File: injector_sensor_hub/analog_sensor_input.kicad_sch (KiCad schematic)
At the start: 24 parts, among them J3 Conn_01x02_Female-Connector, J4 Conn_01x02_Female-Connector, J5 Conn_01x02_Female-Connector, J6 Conn_01x02_Female-Connector

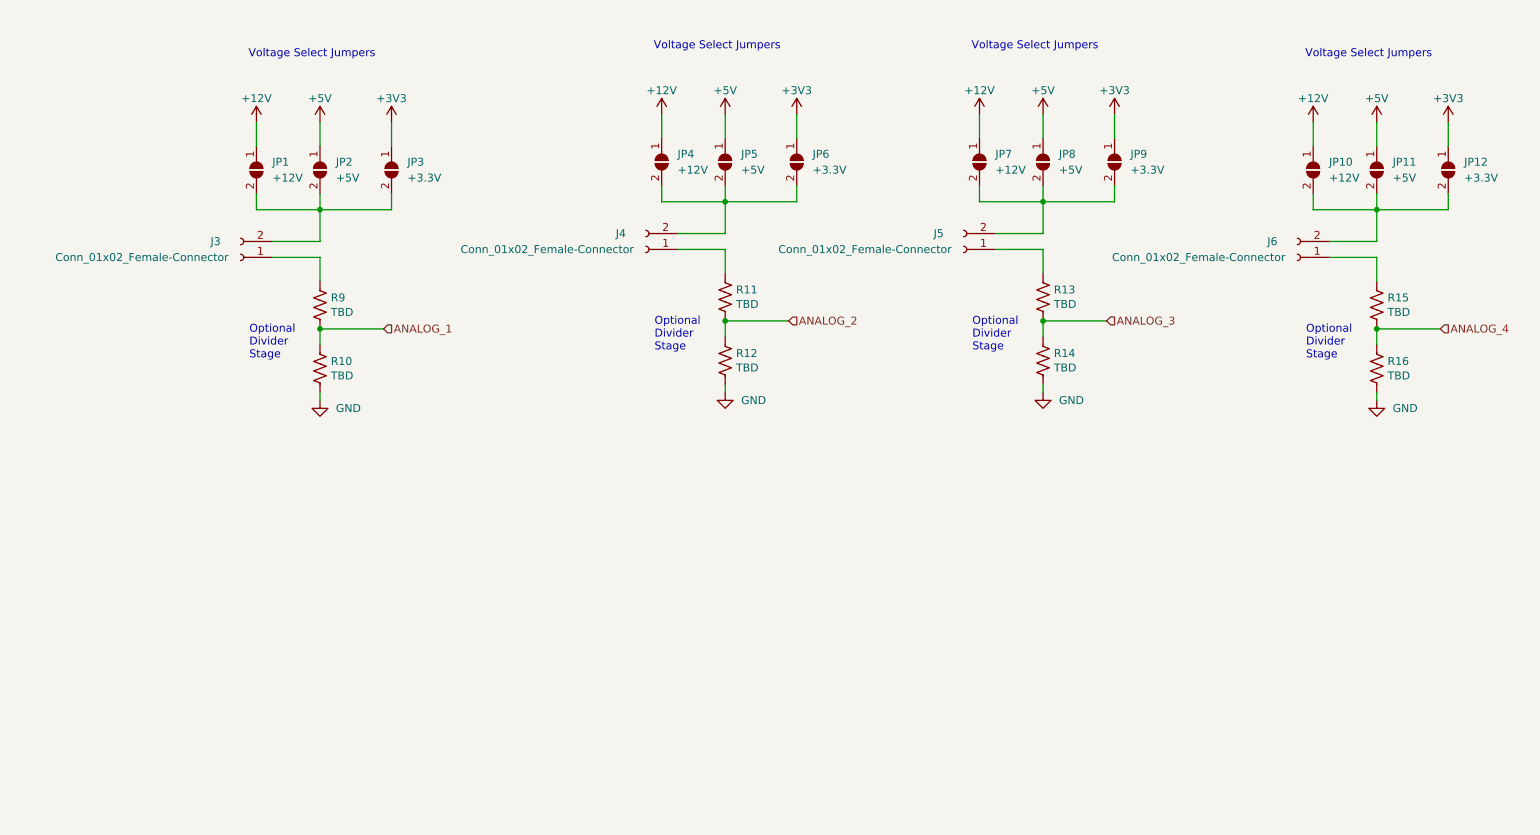
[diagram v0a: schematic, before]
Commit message: Add schematics
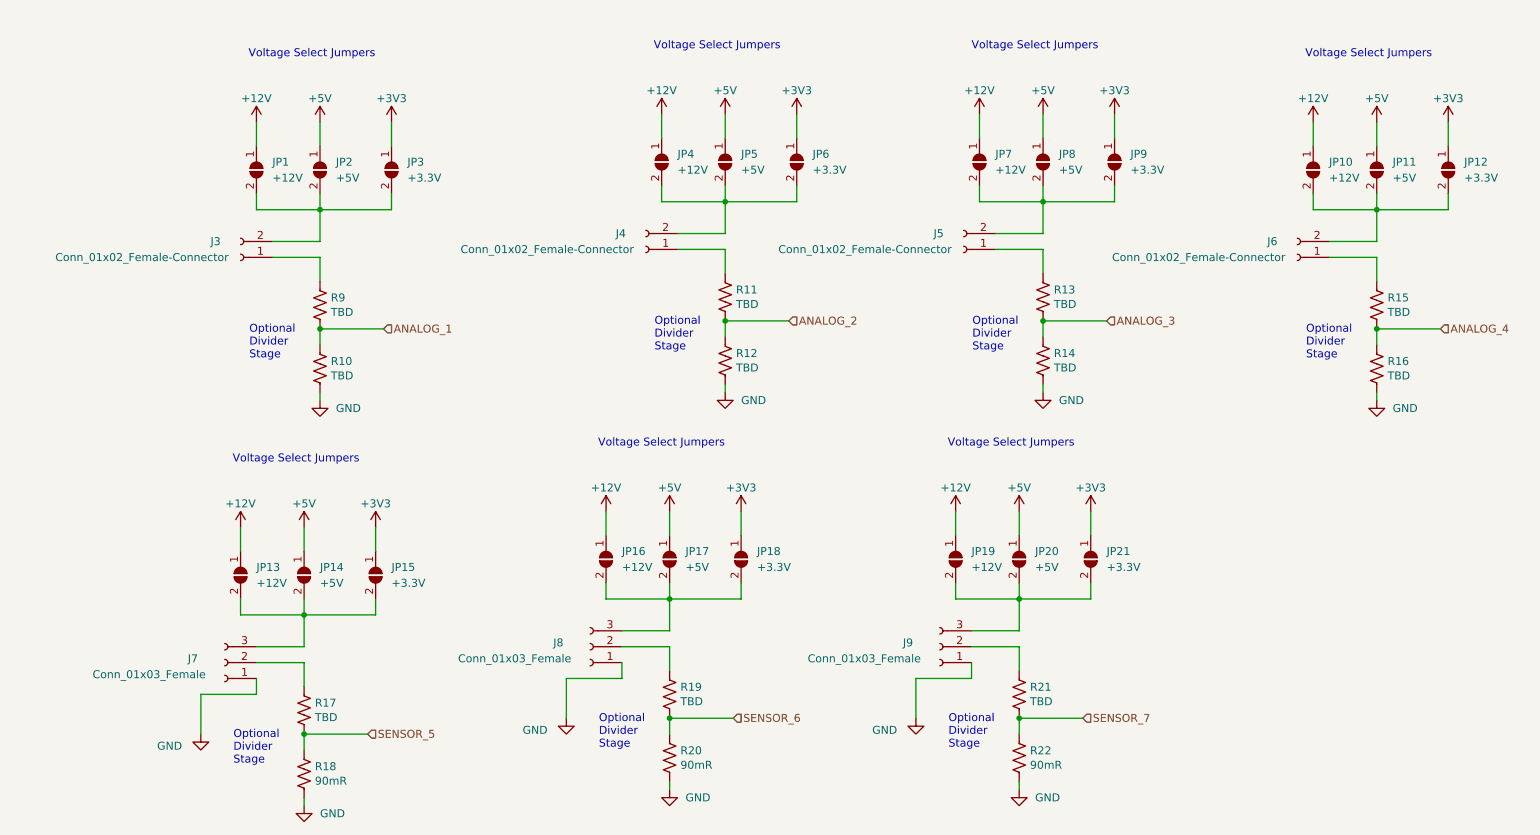
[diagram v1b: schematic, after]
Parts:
- added J7, J8, J9: Conn_01x03_Female, Connector_JST:JST_PH_S3B-PH-K_1x03_P2.00mm_Horizontal, symbol Connector:Conn_01x03_Female
- added JP13, JP16, JP19: +12V, Jumper:SolderJumper-2_P1.3mm_Open_Pad1.0x1.5mm, symbol Jumper:SolderJumper_2_Open
- added JP14, JP17, JP20: +5V, Jumper:SolderJumper-2_P1.3mm_Open_Pad1.0x1.5mm, symbol Jumper:SolderJumper_2_Open
- added JP15, JP18, JP21: +3.3V, Jumper:SolderJumper-2_P1.3mm_Open_Pad1.0x1.5mm, symbol Jumper:SolderJumper_2_Open
- added R17, R19, R21: TBD, Resistor_SMD:R_0805_2012Metric_Pad1.20x1.40mm_HandSolder, symbol Device:R_US
- added R18, R20, R22: 90mR, Resistor_SMD:R_0805_2012Metric_Pad1.20x1.40mm_HandSolder, symbol Device:R_US
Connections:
- net +12V: now also JP13.1 (A), JP16.1 (A), JP19.1 (A)
- net +3V3: now also JP15.1 (A), JP18.1 (A), JP21.1 (A)
- net +5V: now also JP14.1 (A), JP17.1 (A), JP20.1 (A)
- net GND: now also J7.1 (Pin_1), J8.1 (Pin_1), J9.1 (Pin_1), R18.2, R20.2, R22.2
- new net: J7.2 (Pin_2), R17.1
- new net: J8.2 (Pin_2), R19.1
- new net: J8.3 (Pin_3), JP16.2 (B), JP17.2 (B), JP18.2 (B)
- new net: J9.2 (Pin_2), R21.1
- new net: J9.3 (Pin_3), JP19.2 (B), JP20.2 (B), JP21.2 (B)
- new net: J7.3 (Pin_3), JP13.2 (B), JP14.2 (B), JP15.2 (B)
- new net SENSOR_5: R17.2, R18.1
- new net SENSOR_6: R19.2, R20.1
- new net SENSOR_7: R21.2, R22.1

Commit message: updates w ash
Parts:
- added J11: Conn_01x03_Female, Connector_JST:JST_PH_S3B-PH-K_1x03_P2.00mm_Horizontal, symbol Connector:Conn_01x03_Female
- added JP22: +12V, Jumper:SolderJumper-2_P1.3mm_Open_Pad1.0x1.5mm, symbol Jumper:SolderJumper_2_Open
- added JP23: +5V, Jumper:SolderJumper-2_P1.3mm_Open_Pad1.0x1.5mm, symbol Jumper:SolderJumper_2_Open
- added JP24: +3.3V, Jumper:SolderJumper-2_P1.3mm_Open_Pad1.0x1.5mm, symbol Jumper:SolderJumper_2_Open
- added R1: TBD, Resistor_SMD:R_0805_2012Metric_Pad1.20x1.40mm_HandSolder, symbol Device:R_US
- added R2: 90mR, Resistor_SMD:R_0805_2012Metric_Pad1.20x1.40mm_HandSolder, symbol Device:R_US
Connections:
- net +12V: now also JP22.1 (A)
- net +3V3: now also JP24.1 (A)
- net +5V: now also JP23.1 (A)
- net GND: now also J11.1 (Pin_1), R2.2
- new net: J11.2 (Pin_2), R1.1
- new net: J11.3 (Pin_3), JP22.2 (B), JP23.2 (B), JP24.2 (B)
- new net SENSOR_8: R1.2, R2.1

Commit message: final changes, tidy up schematic
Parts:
- R18, R2, R20, R22: value 90mR -> TBD
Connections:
- net ANALOG_1 renamed 2ANALOG_1
- net ANALOG_2 renamed 2ANALOG_2
- net ANALOG_3 renamed 2ANALOG_3
- net ANALOG_4 renamed 2ANALOG_4
- net SENSOR_5 renamed 3ANALOG_1
- net SENSOR_6 renamed 3ANALOG_2
- net SENSOR_7 renamed 3ANALOG_3
- net SENSOR_8 renamed 3ANALOG_4
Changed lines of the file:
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@@
 		)
 	)
-	(hierarchical_label "ANALOG_2"
-		(shape input)
+	(hierarchical_label "3ANALOG_3"
+		(shape output)
+		(at 199.39 134.62 0)
+		(fields_autoplaced yes)
+		(effects
+			(font
+				(size 1.27 1.27)
+			)
+			(justify left)
+		)
+	)
+	(hierarchical_label "3ANALOG_1"
+		(shape output)
+		(at 85.09 137.16 0)
+		(fields_autoplaced yes)
+		(effects
+			(font
+				(size 1.27 1.27)
+			)
+			(justify left)
+		)
+	)
+	(hierarchical_label "3ANALOG_4"
+		(shape output)
+		(at 256.54 135.89 0)
+		(fields_autoplaced yes)
+		(effects
+			(font
+				(size 1.27 1.27)
+			)
+			(justify left)
+		)
+	)
+	(hierarchical_label "2ANALOG_3"
+		(shape output)
+		(at 203.2 71.12 0)
+		(fields_autoplaced yes)
+		(effects
+			(font
+				(size 1.27 1.27)
+			)
+			(justify left)
+		)
+	)
+	(hierarchical_label "2ANALOG_2"
+		(shape output)
 		(at 152.4 71.12 0)
 		(fields_autoplaced yes)
@@
 		)
 	)
-	(hierarchical_label "SENSOR_8"
-		(shape input)
-		(at 256.54 135.89 0)
-		(fields_autoplaced yes)
-		(effects
-			(font
-				(size 1.27 1.27)
-			)
-			(justify left)
-		)
-	)
-	(hierarchical_label "ANALOG_3"
-		(shape input)
-		(at 203.2 71.12 0)
-		(fields_autoplaced yes)
-		(effects
-			(font
-				(size 1.27 1.27)
-			)
-			(justify left)
-		)
-	)
-	(hierarchical_label "SENSOR_5"
-		(shape input)
-		(at 85.09 137.16 0)
-		(fields_autoplaced yes)
-		(effects
-			(font
-				(size 1.27 1.27)
-			)
-			(justify left)
-		)
-	)
-	(hierarchical_label "ANALOG_1"
-		(shape input)
+	(hierarchical_label "2ANALOG_1"
+		(shape output)
 		(at 87.63 72.39 0)
 		(fields_autoplaced yes)
@@
 		)
 	)
-	(hierarchical_label "ANALOG_4"
-		(shape input)
+	(hierarchical_label "3ANALOG_2"
+		(shape output)
+		(at 143.51 134.62 0)
+		(fields_autoplaced yes)
+		(effects
+			(font
+				(size 1.27 1.27)
+			)
+			(justify left)
+		)
+	)
+	(hierarchical_label "2ANALOG_4"
+		(shape output)
 		(at 256.54 72.39 0)
 		(fields_autoplaced yes)
@@
 		)
 	)
-	(hierarchical_label "SENSOR_7"
-		(shape input)
-		(at 199.39 134.62 0)
-		(fields_autoplaced yes)
-		(effects
-			(font
-				(size 1.27 1.27)
-			)
-			(justify left)
-		)
-	)
-	(hierarchical_label "SENSOR_6"
-		(shape input)
-		(at 143.51 134.62 0)
-		(fields_autoplaced yes)
-		(effects
-			(font
-				(size 1.27 1.27)
-			)
-			(justify left)
-		)
-	)
 	(symbol
 		(lib_id "power:GND")
@@
 			)
 		)
-		(property "Value" "90mR"
+		(property "Value" "TBD"
 			(at 135.0772 142.113 0)
 			(effects
@@
 			)
 		)
-		(property "Value" "90mR"
+		(property "Value" "TBD"
 			(at 190.9572 142.113 0)
 			(effects
@@
 			)
 		)
-		(property "Value" "90mR"
+		(property "Value" "TBD"
 			(at 76.6572 144.653 0)
 			(effects
@@
 			)
 		)
-		(property "Value" "90mR"
+		(property "Value" "TBD"
 			(at 248.1072 143.383 0)
 			(effects

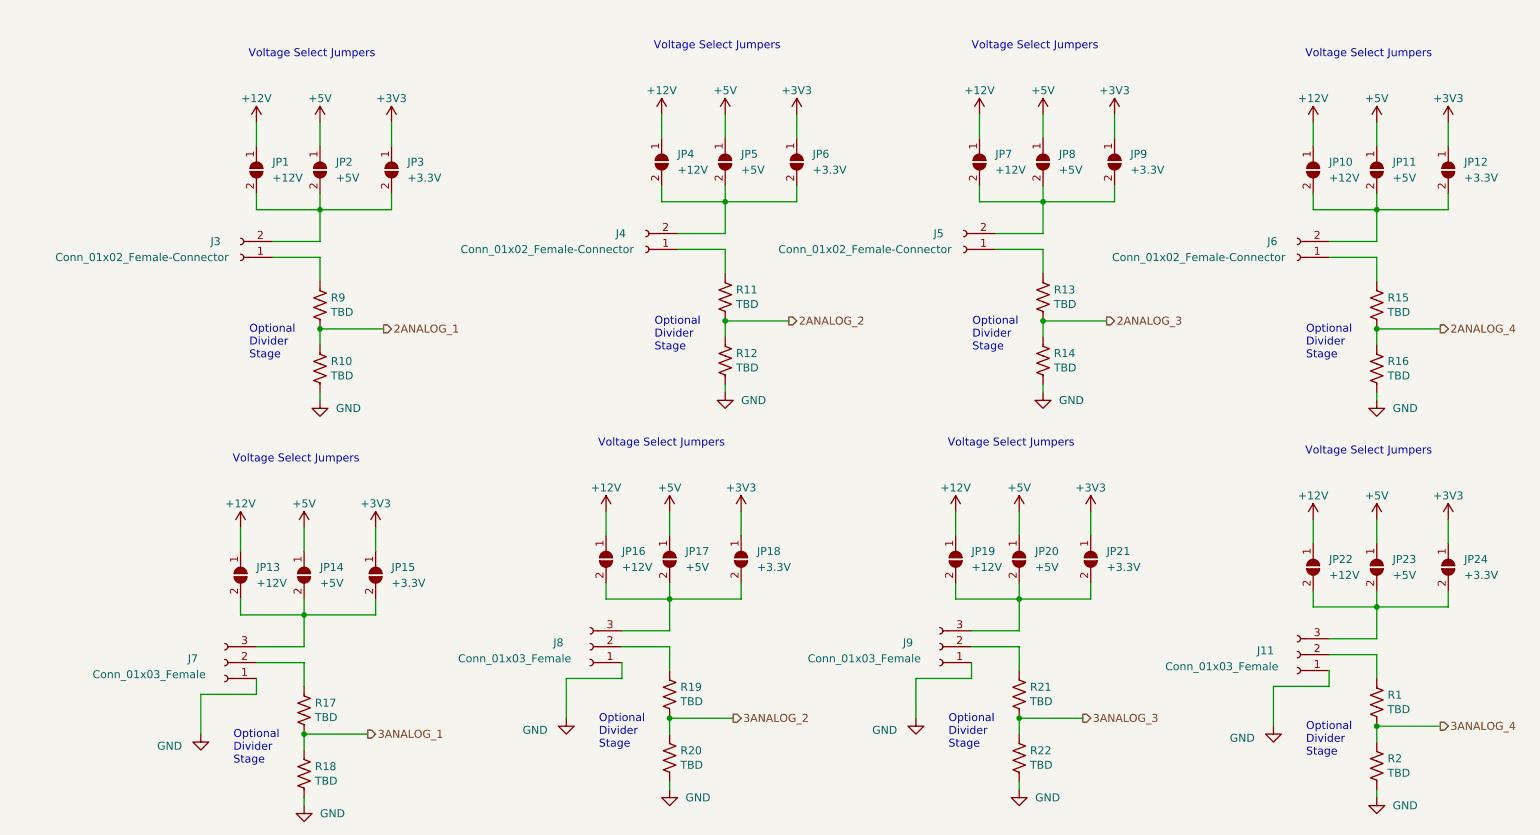
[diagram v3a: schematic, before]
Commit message: changed from 3v3 to 5v
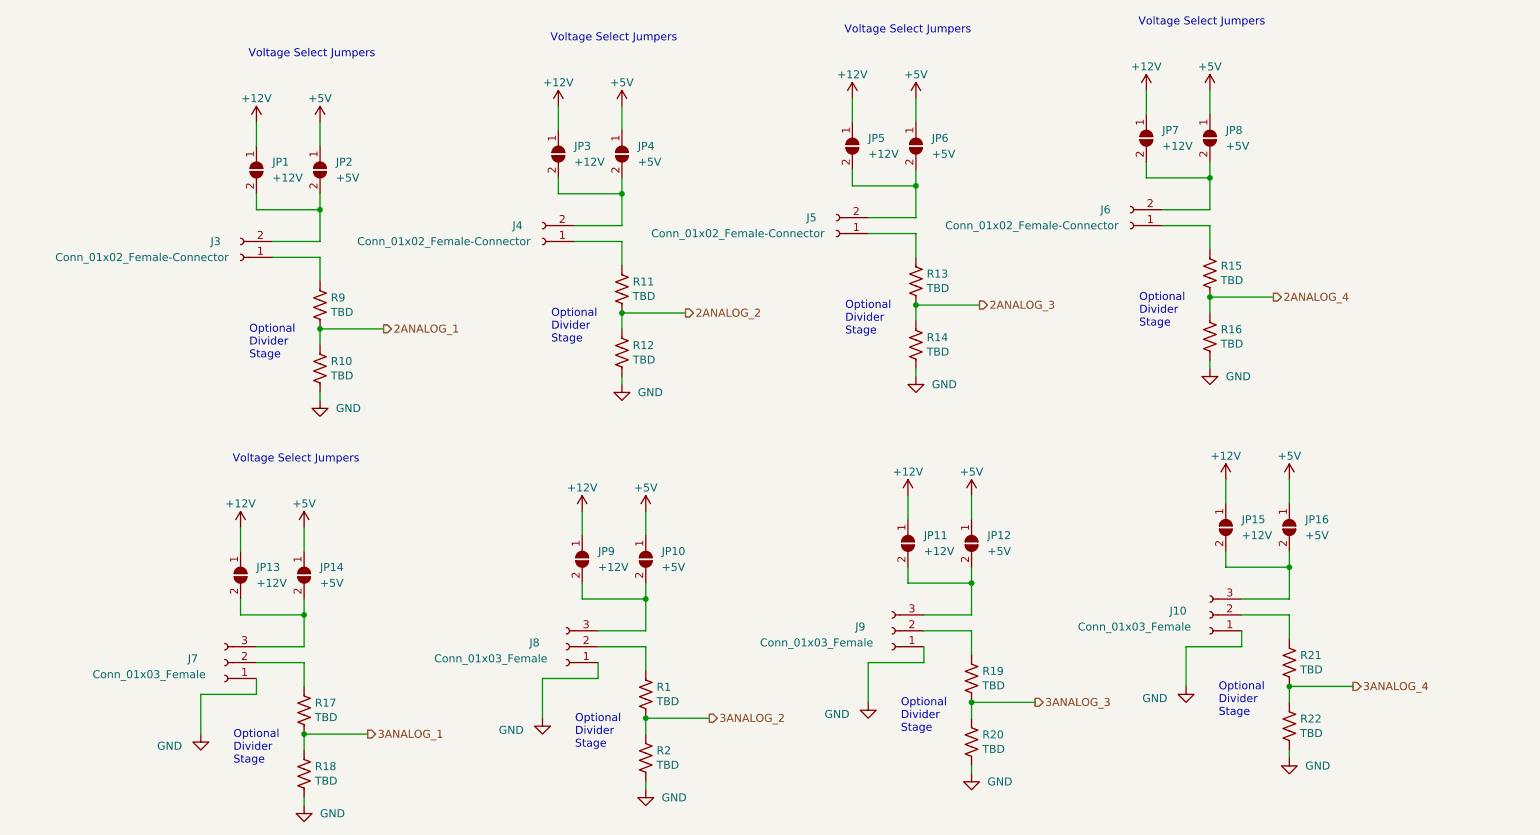
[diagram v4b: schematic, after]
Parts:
- removed J11: Conn_01x03_Female, Connector_JST:JST_PH_S3B-PH-K_1x03_P2.00mm_Horizontal, symbol Connector:Conn_01x03_Female
- removed JP17, JP20, JP23: +5V, Jumper:SolderJumper-2_P1.3mm_Open_Pad1.0x1.5mm, symbol Jumper:SolderJumper_2_Open
- removed JP18, JP21, JP24: +3.3V, Jumper:SolderJumper-2_P1.3mm_Open_Pad1.0x1.5mm, symbol Jumper:SolderJumper_2_Open
- removed JP19, JP22: +12V, Jumper:SolderJumper-2_P1.3mm_Open_Pad1.0x1.5mm, symbol Jumper:SolderJumper_2_Open
- added J10: Conn_01x03_Female, Connector_JST:JST_PH_S3B-PH-K_1x03_P2.00mm_Horizontal, symbol Connector:Conn_01x03_Female
- JP10, JP16, JP4: value +12V -> +5V
- JP11, JP5: value +5V -> +12V
- JP12, JP6: value +3.3V -> +5V
- JP15, JP3, JP9: value +3.3V -> +12V
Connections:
- net +12V: now also JP11.1 (A), JP15.1 (A), JP3.1 (A), JP5.1 (A), JP9.1 (A); no longer JP10.1 (A), JP16.1 (A), JP4.1 (A)
- net +5V: now also JP10.1 (A), JP12.1 (A), JP16.1 (A), JP4.1 (A), JP6.1 (A); no longer JP11.1 (A), JP5.1 (A)
- net 3ANALOG_2: now also R1.2, R2.1; no longer R19.2, R20.1
- net 3ANALOG_3: now also R19.2, R20.1; no longer R21.2, R22.1
- net 3ANALOG_4: now also R21.2, R22.1; no longer R1.2, R2.1
- net GND: now also J10.1 (Pin_1)
- net at J3.2 (Pin_2), JP1.2 (B), JP2.2 (B): no longer JP3.2 (B)
- net at R1.1: now also J8.2 (Pin_2)
- net at R19.1: now also J9.2 (Pin_2); no longer J8.2 (Pin_2)
- net at J8.3 (Pin_3): now also JP10.2 (B), JP9.2 (B); no longer JP16.2 (B)
- net at R21.1: now also J10.2 (Pin_2); no longer J9.2 (Pin_2)
- net at J9.3 (Pin_3): now also JP11.2 (B), JP12.2 (B)
- net at J4.2 (Pin_2), JP4.2 (B): now also JP3.2 (B); no longer JP5.2 (B), JP6.2 (B)
- net at JP7.2 (B), JP8.2 (B): now also J6.2 (Pin_2); no longer J5.2 (Pin_2), JP9.2 (B)
- net at J7.3 (Pin_3), JP13.2 (B), JP14.2 (B): no longer JP15.2 (B)
- removed net +3V3: JP12.1 (A), JP15.1 (A), JP3.1 (A), JP6.1 (A), JP9.1 (A)
- new net: J5.2 (Pin_2), JP5.2 (B), JP6.2 (B)
- new net: J10.3 (Pin_3), JP15.2 (B), JP16.2 (B)

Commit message: revert changes to daq and propulsion board
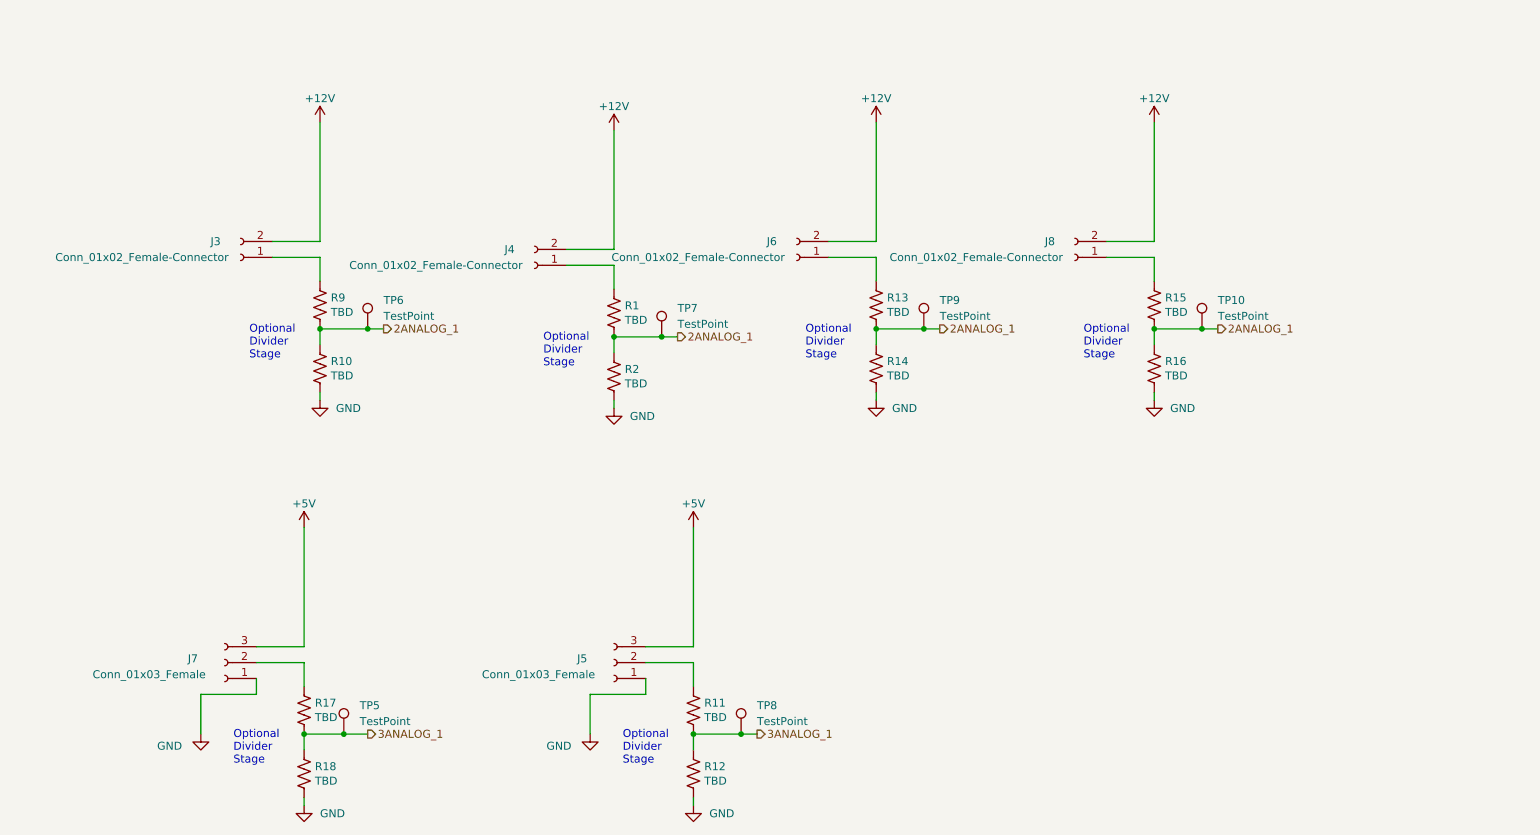
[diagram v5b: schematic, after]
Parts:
- removed J10, J8, J9: Conn_01x03_Female, Connector_JST:JST_PH_S3B-PH-K_1x03_P2.00mm_Horizontal, symbol Connector:Conn_01x03_Female
- removed J5: Conn_01x02_Female-Connector, Connector_JST:JST_PH_S2B-PH-K_1x02_P2.00mm_Horizontal, symbol Connector:Conn_01x02_Female
- removed JP1, JP11, JP13, JP15, JP3, JP5, JP7, JP9: +12V, Jumper:SolderJumper-2_P1.3mm_Open_Pad1.0x1.5mm, symbol Jumper:SolderJumper_2_Open
- removed JP10, JP12, JP14, JP16, JP2, JP4, JP6, JP8: +5V, Jumper:SolderJumper-2_P1.3mm_Open_Pad1.0x1.5mm, symbol Jumper:SolderJumper_2_Open
- removed R19, R20, R21, R22: TBD, Resistor_SMD:R_0805_2012Metric_Pad1.20x1.40mm_HandSolder, symbol Device:R_US
- added J5: Conn_01x03_Female, Connector_JST:JST_PH_S3B-PH-K_1x03_P2.00mm_Horizontal, symbol Connector:Conn_01x03_Female
- added J8: Conn_01x02_Female-Connector, Connector_JST:JST_PH_S2B-PH-K_1x02_P2.00mm_Horizontal, symbol Connector:Conn_01x02_Female
- added TP10, TP5, TP6, TP7, TP8, TP9: TestPoint, symbol Connector:TestPoint
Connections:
- net 2ANALOG_2 is gone; now on net 3ANALOG_1: R11.2, R12.1
- net 2ANALOG_3 is gone; now on net 2ANALOG_1: R13.2, R14.1
- net 2ANALOG_4 is gone; now on net 2ANALOG_1: R15.2, R16.1
- net 3ANALOG_2 is gone; now on net 2ANALOG_1: R1.2, R2.1
- net +12V: now also J3.2 (Pin_2), J4.2 (Pin_2), J6.2 (Pin_2), J8.2 (Pin_2)
- net +5V: now also J7.3 (Pin_3), J5.3 (Pin_3)
- net 2ANALOG_1: now also TP10.1, TP6.1, TP7.1, TP9.1
- net 3ANALOG_1: now also TP5.1, TP8.1
- net GND: now also J5.1 (Pin_1)
- net at R13.1: now also J6.1 (Pin_1)
- net at R15.1: now also J8.1 (Pin_1); no longer J6.1 (Pin_1)
- net at R1.1: now also J4.1 (Pin_1)
- net at R11.1: now also J5.2 (Pin_2); no longer J4.1 (Pin_1)
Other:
- note removed: "Voltage Select Jumpers"

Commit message: fixed J1 connector to right pins and cleaned up schematic wiring
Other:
- title: (none) -> Injector Sensor Hub 
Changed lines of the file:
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@@
 	(generator_version "8.0")
 	(paper "A4")
+	(title_block
+		(title "Injector Sensor Hub ")
+	)
 	(junction
 		(at 85.09 72.39)
